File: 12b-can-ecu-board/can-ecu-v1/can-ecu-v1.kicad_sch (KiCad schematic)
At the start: 42 parts, among them J1 USB_C_Receptacle_USB2.0_14P, J2 Conn_01x05, J3 Conn_01x04, J4 Conn_01x03, SW1 SW_Push, SW2 SW_Push, SW3 SW_Push, U1 STM32F407VGTx, U2 AMS1117-3.3, U3 SN65HVD230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

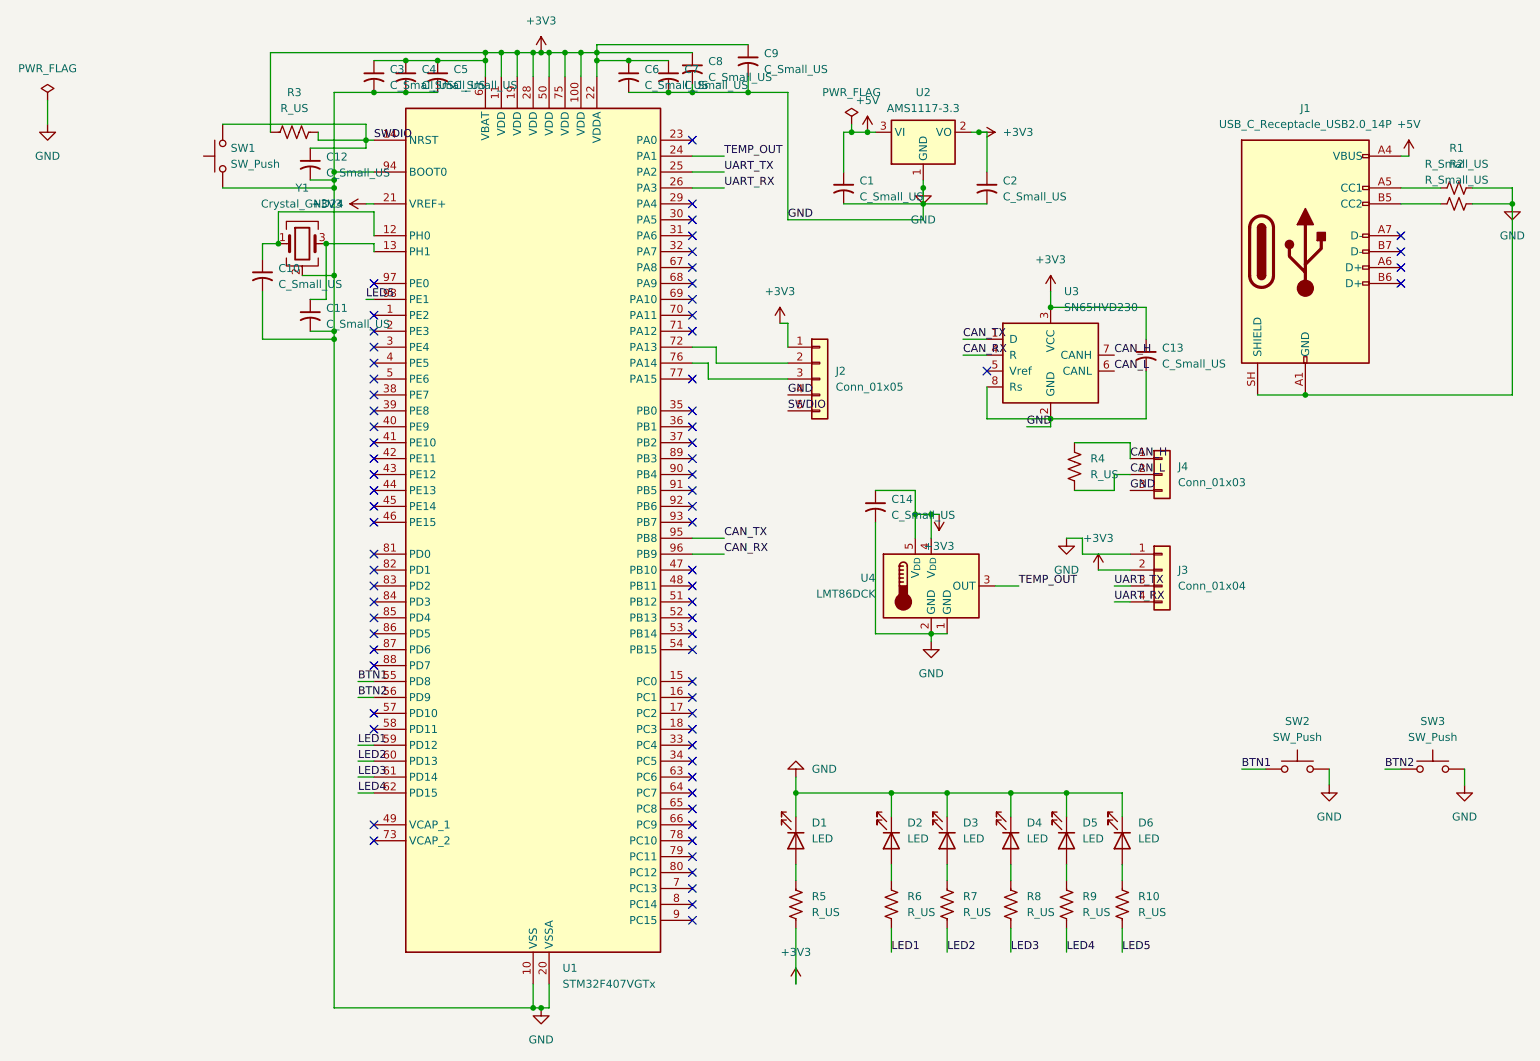
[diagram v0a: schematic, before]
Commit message: 12b-can-ecu-board: footprints assigned, LCSC numbers and values set
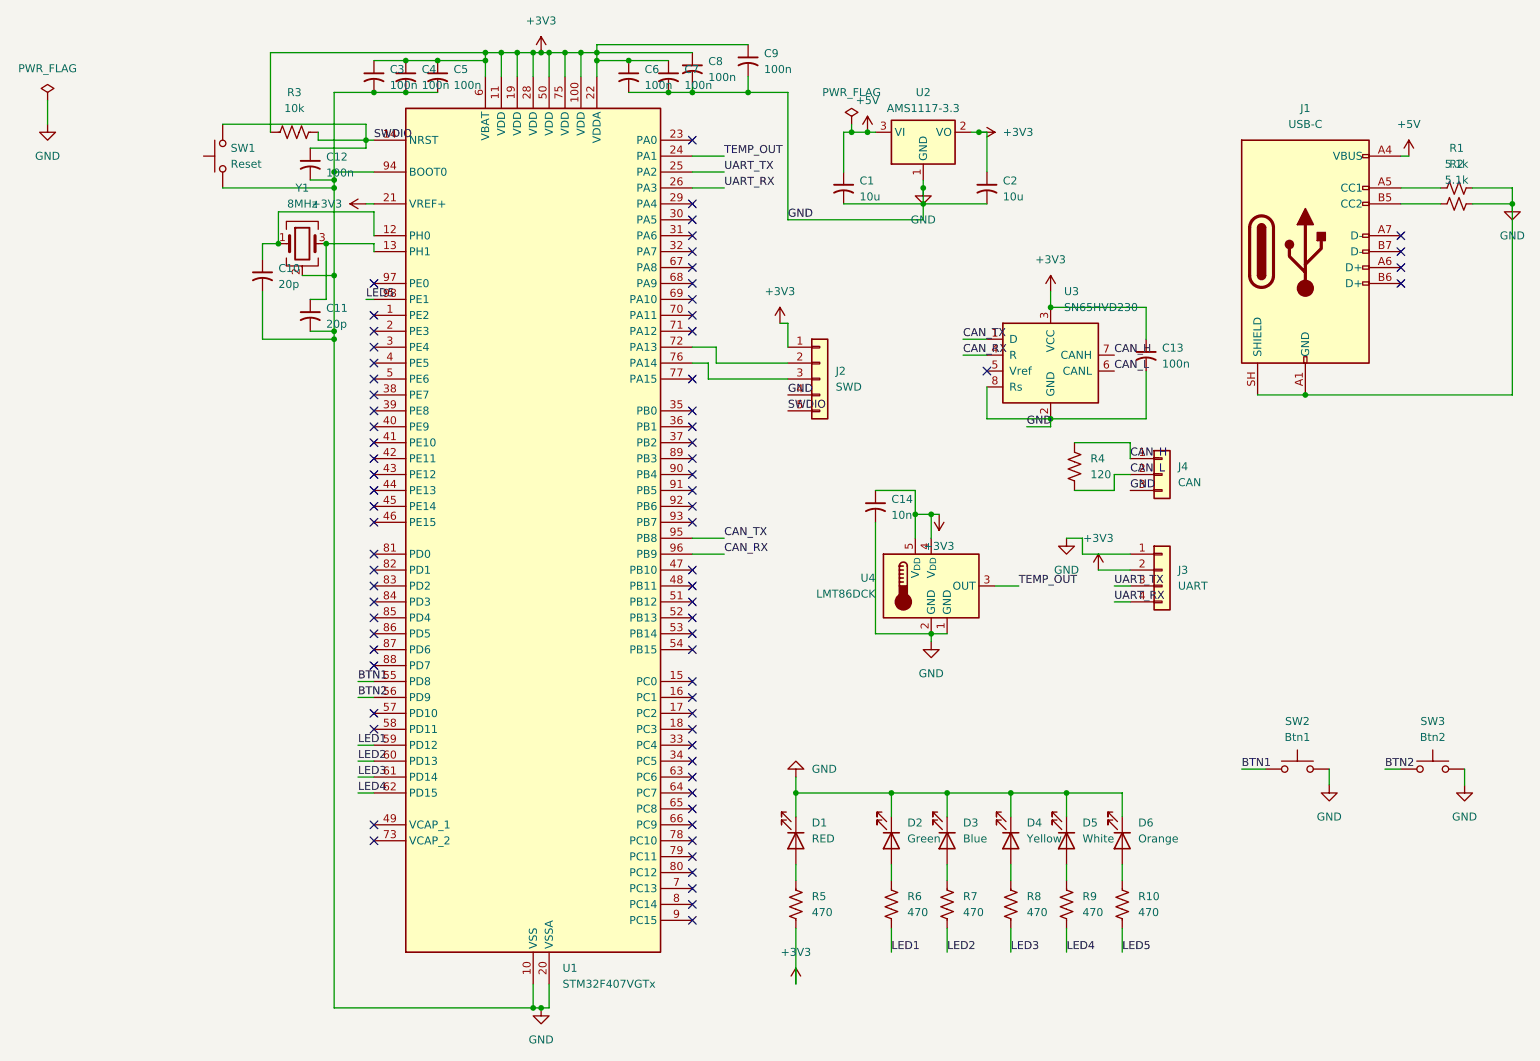
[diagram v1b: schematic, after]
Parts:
- C1, C2: value C_Small_US -> 10u; footprint (none) -> Capacitor_SMD:C_0603_1608Metric; LCSC (none) -> C19702
- C10, C11: value C_Small_US -> 20p; footprint (none) -> Capacitor_SMD:C_0603_1608Metric; LCSC (none) -> C1804
- C12, C13, C3, C4, C5, C6, C7, C8, C9: value C_Small_US -> 100n; footprint (none) -> Capacitor_SMD:C_0603_1608Metric; LCSC (none) -> C14663
- C14: value C_Small_US -> 10n; footprint (none) -> Capacitor_SMD:C_0603_1608Metric; LCSC (none) -> C57112
- D1: value LED -> RED; footprint (none) -> LED_SMD:LED_0603_1608Metric; LCSC (none) -> C2286
- D2: value LED -> Green; footprint (none) -> LED_SMD:LED_0603_1608Metric; LCSC (none) -> C72043
- D3: value LED -> Blue; footprint (none) -> LED_SMD:LED_0603_1608Metric; LCSC (none) -> C72041
- D4: value LED -> Yellow; footprint (none) -> LED_SMD:LED_0603_1608Metric; LCSC (none) -> C72038
- D5: value LED -> White; footprint (none) -> LED_SMD:LED_0603_1608Metric; LCSC (none) -> C2290
- D6: value LED -> Orange; footprint (none) -> LED_SMD:LED_0603_1608Metric; LCSC (none) -> C12624
- J1: value USB_C_Receptacle_USB2.0_14P -> USB-C; footprint (none) -> Connector_USB:USB_C_Receptacle_GCT_USB4135-GF-A_6P_TopMnt_Horizontal; LCSC (none) -> C2765186
- J2: value Conn_01x05 -> SWD; footprint (none) -> Connector_PinHeader_2.54mm:PinHeader_1x05_P2.54mm_Vertical; LCSC (none) -> C50982
- J3: value Conn_01x04 -> UART; footprint (none) -> Connector_PinHeader_2.54mm:PinHeader_1x04_P2.54mm_Vertical; LCSC (none) -> C50981
- J4: value Conn_01x03 -> CAN; footprint (none) -> Connector_PinHeader_2.54mm:PinHeader_1x03_P2.54mm_Vertical; LCSC (none) -> C50980
- R1, R2: value R_Small_US -> 5.1k; footprint (none) -> Resistor_SMD:R_0603_1608Metric; LCSC (none) -> C23186
- R10, R5, R6, R7, R8, R9: value R_US -> 470; footprint (none) -> Resistor_SMD:R_0603_1608Metric; LCSC (none) -> C23179
- R3: value R_US -> 10k; footprint (none) -> Resistor_SMD:R_0603_1608Metric; LCSC (none) -> C25804
- R4: value R_US -> 120; footprint (none) -> Resistor_SMD:R_0603_1608Metric; LCSC (none) -> C22787
- SW1: value SW_Push -> Reset; footprint (none) -> Button_Switch_SMD:SW_SPST_PTS645Sx43SMTR92; LCSC (none) -> C318884
- SW2: value SW_Push -> Btn1; footprint (none) -> Button_Switch_SMD:SW_SPST_PTS645Sx43SMTR92; LCSC (none) -> C318884
- SW3: value SW_Push -> Btn2; footprint (none) -> Button_Switch_SMD:SW_SPST_PTS645Sx43SMTR92; LCSC (none) -> C318884
- U1: LCSC (none) -> C12345
- U2: LCSC (none) -> C6186
- U3: LCSC (none) -> C12084
- U4: LCSC (none) -> C133909
- Y1: value Crystal_GND24 -> 8MHz; footprint (none) -> Crystal:Crystal_SMD_3225-4Pin_3.2x2.5mm; LCSC (none) -> C115962

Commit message: 12b-can-ecu-board: first attempt at the schematic. restarting bc errors
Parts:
- J1: symbol Connector:USB_C_Receptacle_USB2.0_14P -> Connector:USB_C_Receptacle_PowerOnly_6P
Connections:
- net +5V: no longer J1.A4 (VBUS), J1.B4 (VBUS)
- net GND: no longer J1.A1 (GND), J1.B1 (GND)
- no-connect marks 73 -> 69
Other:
- moved on the sheet: R1, R2
